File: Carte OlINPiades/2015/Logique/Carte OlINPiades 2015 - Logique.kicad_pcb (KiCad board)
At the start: 2 copper layers, 30 parts, among them U1 dsPIC33FJ128MC802, U2 LM7805, U3 LM2937-3.3

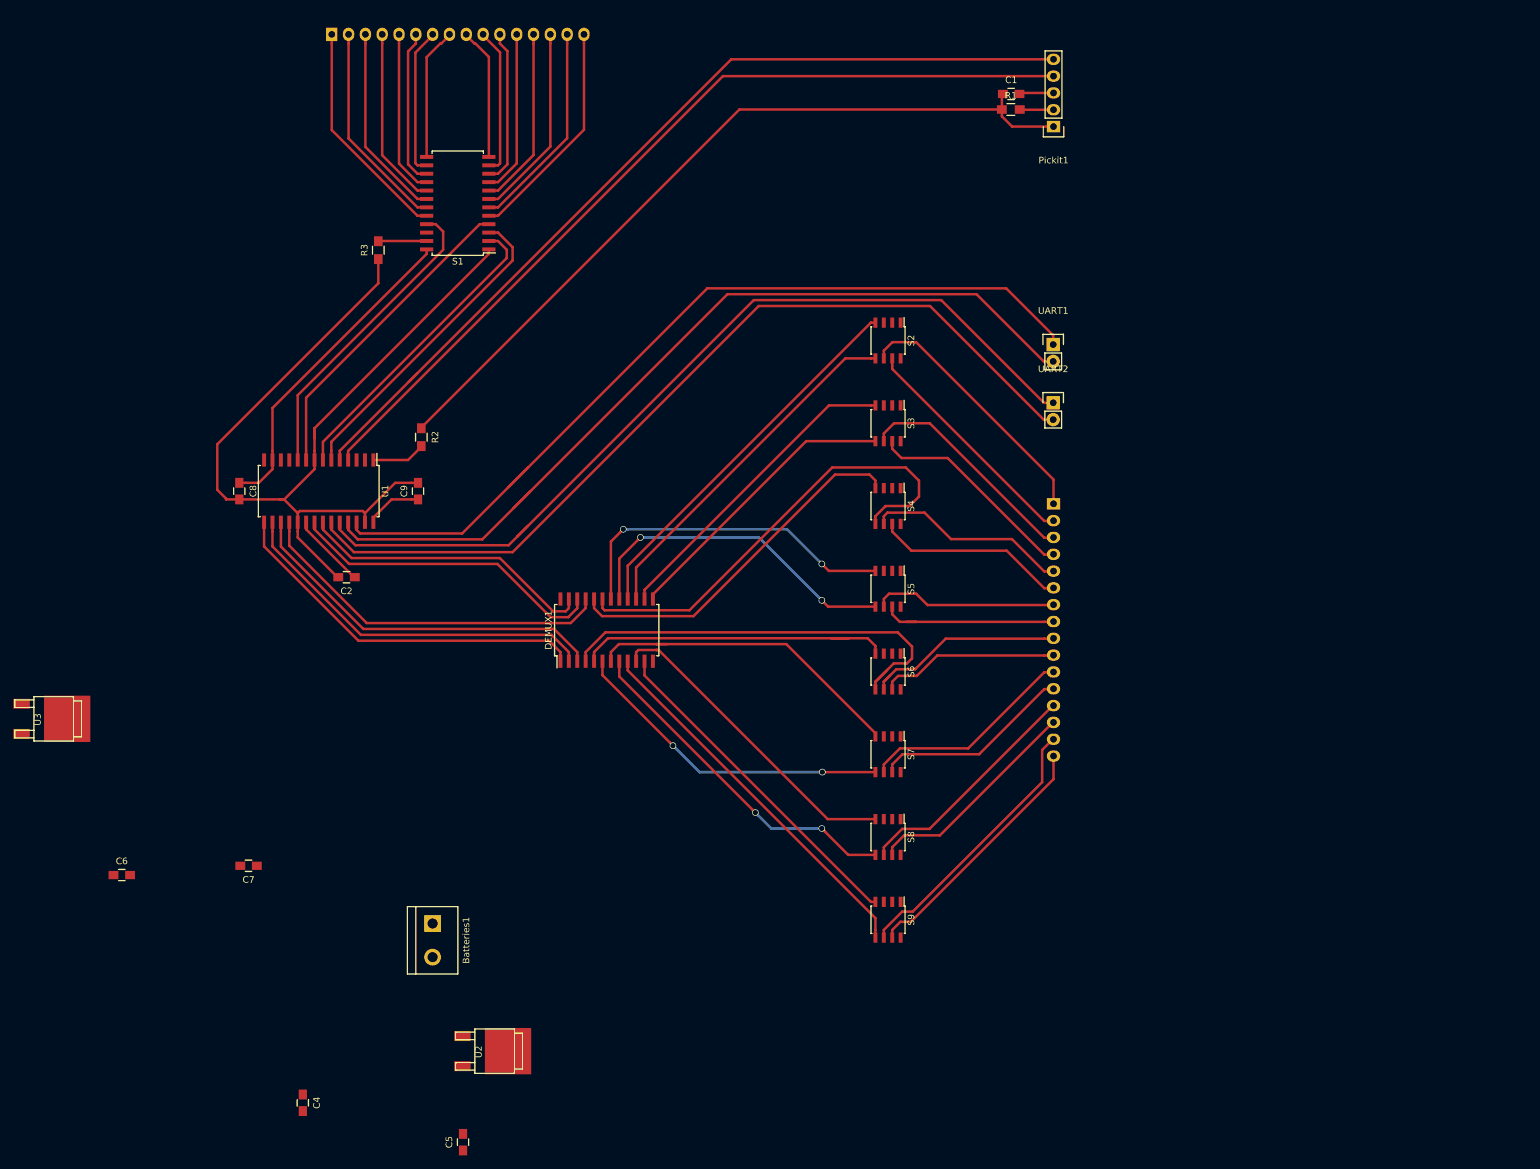
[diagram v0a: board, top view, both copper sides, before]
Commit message: déplace les composant d'alim dans leur zone
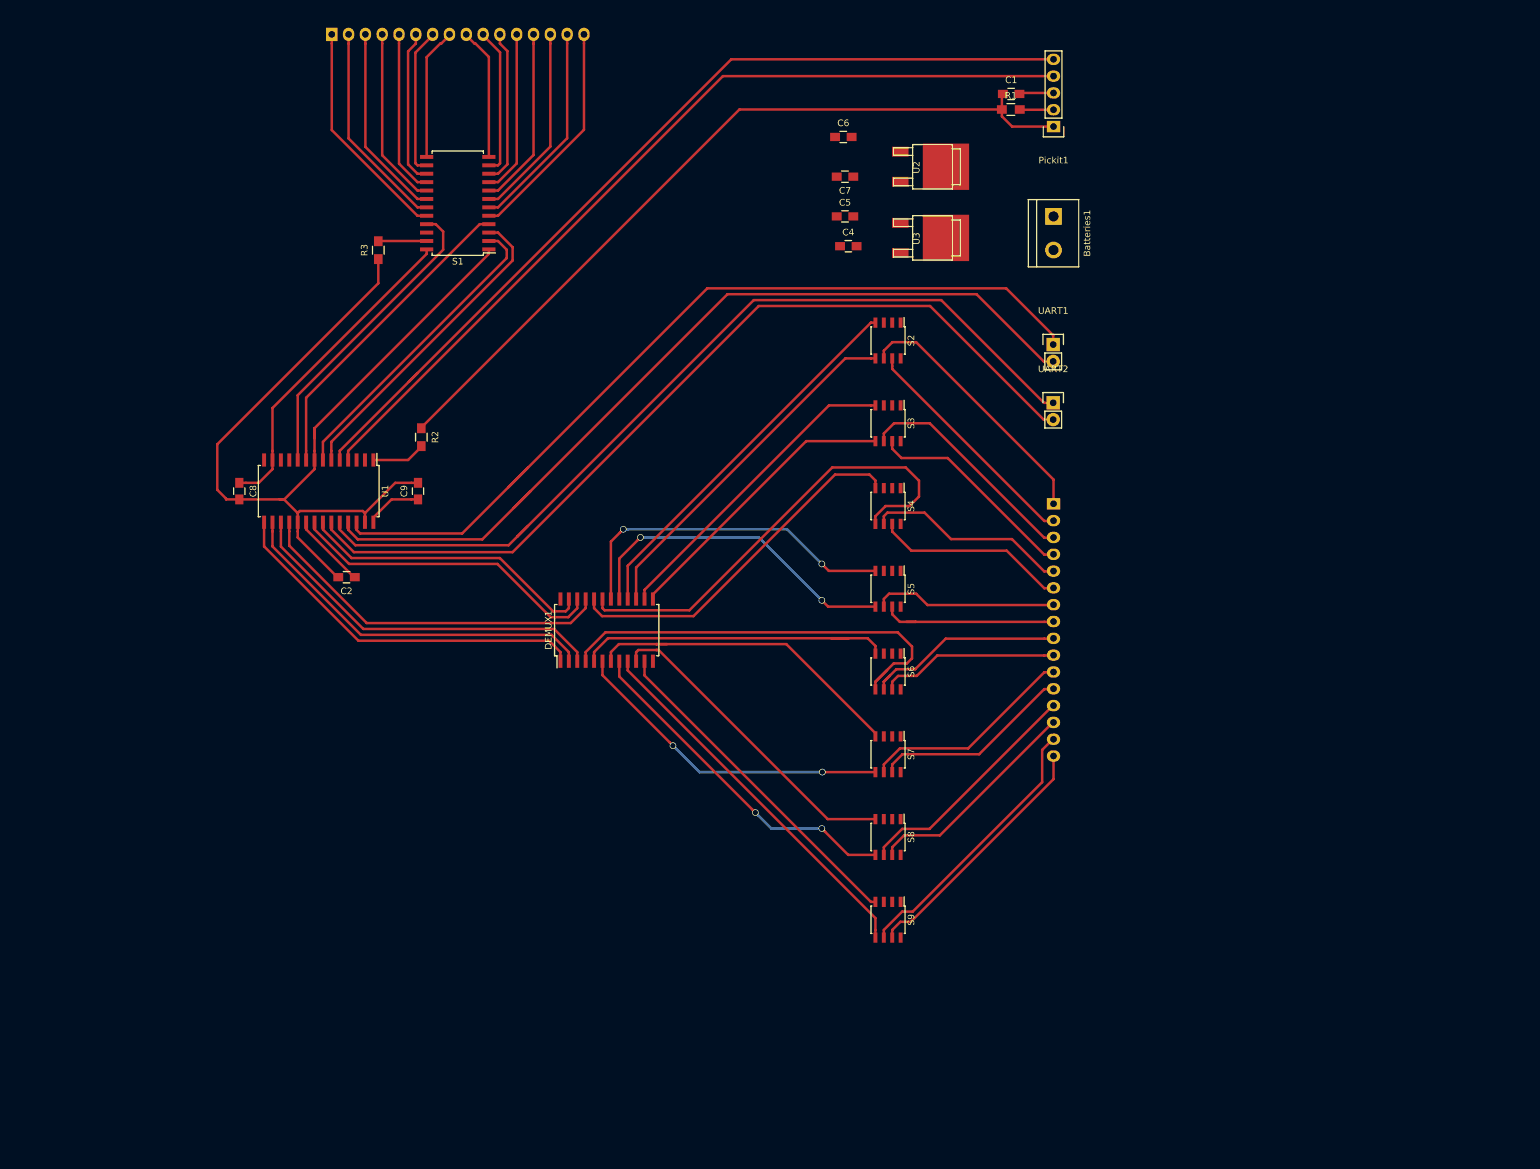
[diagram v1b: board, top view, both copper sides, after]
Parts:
- moved C6 155.9 mm to (198.2, 25.5)
- moved C4 153.4 mm to (199.0, 42.0), turned to 0 degrees
- moved U3 151.3 mm to (210.3, 40.8)
- moved C5 151.3 mm to (198.5, 37.5), turned to 0 degrees
- moved U2 149.1 mm to (210.3, 30.0)
- moved Batteries1 142.2 mm to (230.0, 40.0)
- moved C7 137.7 mm to (198.5, 31.5)
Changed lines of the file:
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@@
     (visible_elements FFFFFF7F)
     (pcbplotparams
-      (layerselection 0x00030_80000001)
+      (layerselection 0x3c000_00000001)
       (usegerberextensions false)
       (excludeedgelayer true)
@@
       (outputformat 1)
       (mirror false)
-      (drillshape 1)
+      (drillshape 0)
       (scaleselection 1)
       (outputdirectory ""))
@@
   )
   (module Capacitors_SMD:C_0805_HandSoldering (layer F.Cu)
-    (at 108.4 135.6 180)
+    (at 198.5 31.5 180)
     (descr "Capacitor SMD 0805, hand soldering")
     (tags "capacitor 0805")
@@
   )
   (module Connect:bornier2 (layer F.Cu)
-    (at 136.2 146.86 270)
+    (at 230 40.04 270)
     (descr "Bornier d'alimentation 2 pins")
     (tags DEV)
@@
   )
   (module Capacitors_SMD:C_0805_HandSoldering (layer F.Cu)
-    (at 116.6 171.4 270)
+    (at 199 42)
     (descr "Capacitor SMD 0805, hand soldering")
     (tags "capacitor 0805")
     (attr smd)
-    (fp_text reference C4 (at 0 -2.1 270) (layer F.SilkS)
-      (effects (font (size 1 1) (thickness 0.15)))
-    )
-    (fp_text value 330nF (at 0 2.1 270) (layer F.Fab)
+    (fp_text reference C4 (at 0 -2.1) (layer F.SilkS)
+      (effects (font (size 1 1) (thickness 0.15)))
+    )
+    (fp_text value 330nF (at 0 2.1) (layer F.Fab)
       (effects (font (size 1 1) (thickness 0.15)))
     )
@@
     (fp_line (start 0.5 -0.85) (end -0.5 -0.85) (layer F.SilkS) (width 0.15))
     (fp_line (start -0.5 0.85) (end 0.5 0.85) (layer F.SilkS) (width 0.15))
-    (pad 1 smd rect (at -1.25 0 270) (size 1.5 1.25) (layers F.Cu F.Paste F.Mask)
+    (pad 1 smd rect (at -1.25 0) (size 1.5 1.25) (layers F.Cu F.Paste F.Mask)
       (net 1 +12V))
-    (pad 2 smd rect (at 1.25 0 270) (size 1.5 1.25) (layers F.Cu F.Paste F.Mask)
+    (pad 2 smd rect (at 1.25 0) (size 1.5 1.25) (layers F.Cu F.Paste F.Mask)
       (net 2 GND))
     (model Capacitors_SMD.3dshapes/C_0805_HandSoldering.wrl
@@
   )
   (module Capacitors_SMD:C_0805_HandSoldering (layer F.Cu)
-    (at 140.8 177.35 90)
+    (at 198.5 37.5)
     (descr "Capacitor SMD 0805, hand soldering")
     (tags "capacitor 0805")
     (attr smd)
-    (fp_text reference C5 (at 0 -2.1 90) (layer F.SilkS)
-      (effects (font (size 1 1) (thickness 0.15)))
-    )
-    (fp_text value 100nF (at 0 2.1 90) (layer F.Fab)
+    (fp_text reference C5 (at 0 -2.1) (layer F.SilkS)
+      (effects (font (size 1 1) (thickness 0.15)))
+    )
+    (fp_text value 100nF (at 0 2.1) (layer F.Fab)
       (effects (font (size 1 1) (thickness 0.15)))
     )
@@
     (fp_line (start 0.5 -0.85) (end -0.5 -0.85) (layer F.SilkS) (width 0.15))
     (fp_line (start -0.5 0.85) (end 0.5 0.85) (layer F.SilkS) (width 0.15))
-    (pad 1 smd rect (at -1.25 0 90) (size 1.5 1.25) (layers F.Cu F.Paste F.Mask)
-      (net 47 +5V))
-    (pad 2 smd rect (at 1.25 0 90) (size 1.5 1.25) (layers F.Cu F.Paste F.Mask)
+    (pad 1 smd rect (at -1.25 0) (size 1.5 1.25) (layers F.Cu F.Paste F.Mask)
+      (net 47 +5V))
+    (pad 2 smd rect (at 1.25 0) (size 1.5 1.25) (layers F.Cu F.Paste F.Mask)
       (net 2 GND))
     (model Capacitors_SMD.3dshapes/C_0805_HandSoldering.wrl
@@
   )
   (module Capacitors_SMD:C_0805_HandSoldering (layer F.Cu)
-    (at 89.25 137)
+    (at 198.25 25.5)
     (descr "Capacitor SMD 0805, hand soldering")
     (tags "capacitor 0805")
@@
   )
   (module Transistors_SMD:sot428 (layer F.Cu)
-    (at 144.15068 163.6 270)
+    (at 210.30068 30 270)
     (descr SOT428)
     (attr smd)
@@
   )
   (module Transistors_SMD:sot428 (layer F.Cu)
-    (at 77.55068 113.4 270)
+    (at 210.30068 40.75 270)
     (descr SOT428)
     (attr smd)

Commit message: connection logique avec regul ok
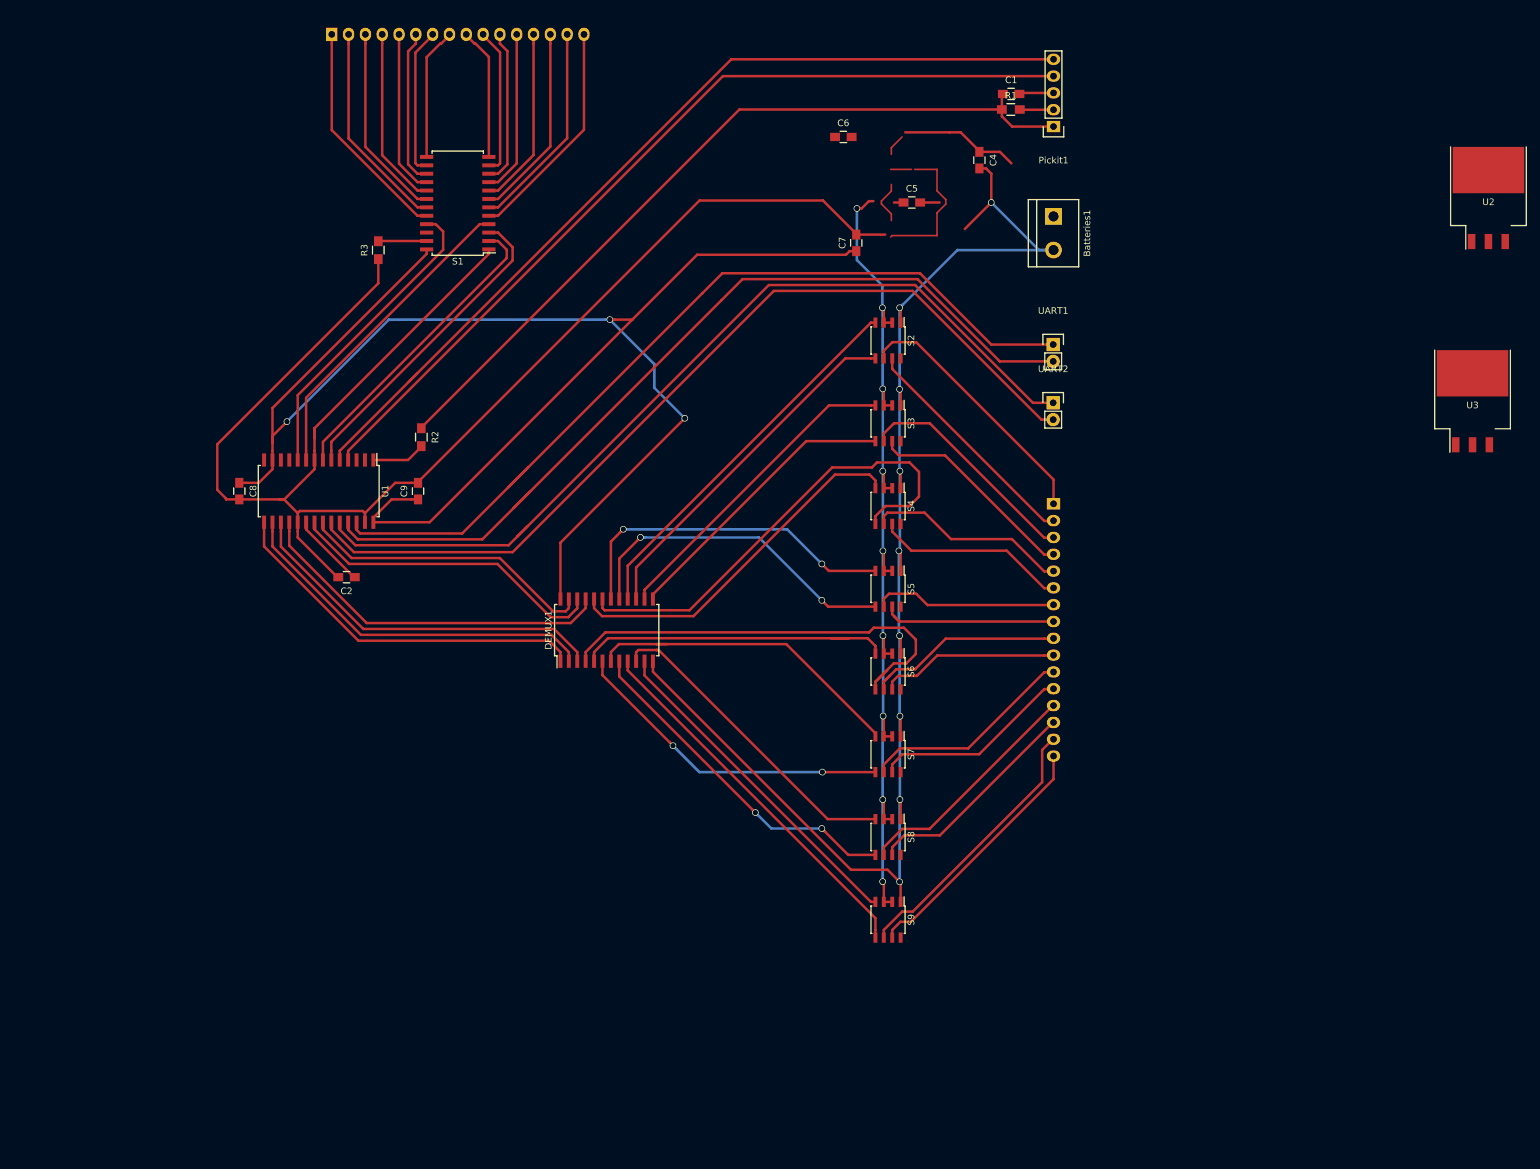
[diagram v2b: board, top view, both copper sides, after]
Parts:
- U2: value LM7805 -> 7805; footprint Transistors_SMD:sot428 -> SMD_Packages:TO-263
- U3: footprint Transistors_SMD:sot428 -> SMD_Packages:TO-263
- moved U3 88.7 mm to (293.3, 72.0), turned to 0 degrees
- moved U2 86.1 mm to (295.7, 41.3), turned to 0 degrees
- moved C4 23.7 mm to (218.8, 29.0), turned to 270 degrees
- moved C5 10.3 mm to (208.6, 35.4)
- moved C7 10.1 mm to (200.2, 41.5), turned to 90 degrees
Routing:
- net GND: track 150.6 -> 457.1 mm, vias 0 -> 9
- net +3.3V: track 62.6 -> 269.8 mm, vias 0 -> 3
- net +5V: track 0.00 -> 140.6 mm, vias 0 -> 9
- net (no net): track 0.00 -> 34.7 mm
- net +12V: track 0.00 -> 18.0 mm
- net Net-(DEMUX1-Pad4): track 65.2 -> 67.2 mm
- net RB14: track 131.3 -> 133.2 mm
- net RB12: track 134.1 -> 136.0 mm
- net RB13: track 133.9 -> 135.8 mm
- net Net-(DEMUX1-Pad19): track 70.5 -> 71.9 mm
- net RB15: track 130.4 -> 131.5 mm

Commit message: cablage alim
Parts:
- removed C5: 100nF, Capacitors_SMD:C_0805_HandSoldering
- C4, C6, C7, U2, U3: moved to B.Cu
- moved U3 104.9 mm to (194.2, 37.6), turned to 180 degrees
- moved U2 88.0 mm to (207.8, 37.6), turned to 180 degrees
- moved C6 13.1 mm to (201.0, 38.3), turned to 90 degrees
- moved C4 11.2 mm to (217.4, 40.1)
- moved C7 7.20 mm to (193.0, 41.5), turned to 0 degrees
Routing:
- net GND: track 457.1 -> 701.7 mm
- net +3.3V: track 269.8 -> 341.9 mm
- net (no net): track 34.7 -> 0.00 mm
- net +12V: track 18.0 -> 21.1 mm
- net +5V: track 140.6 -> 143.3 mm, vias 9 -> 8

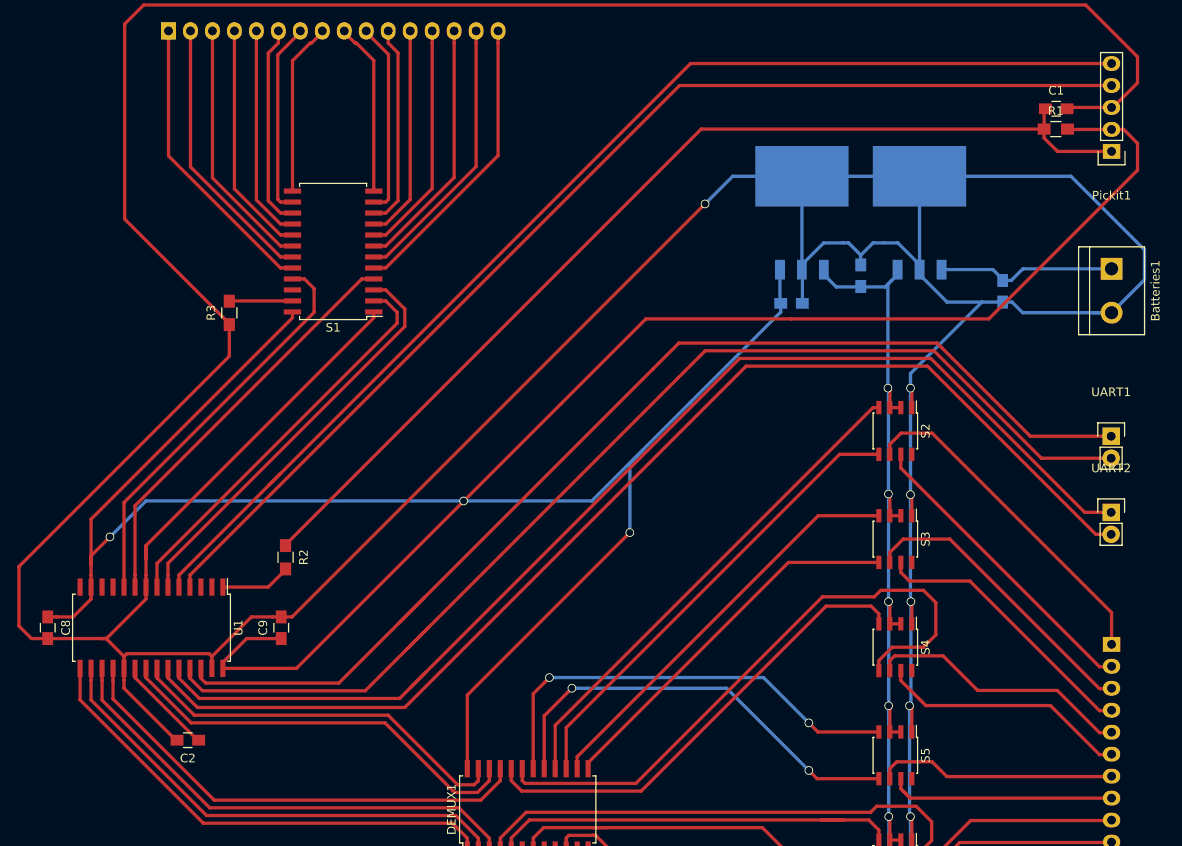
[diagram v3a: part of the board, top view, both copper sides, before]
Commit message: DRC ok sauf pour connecteur d'UART ?
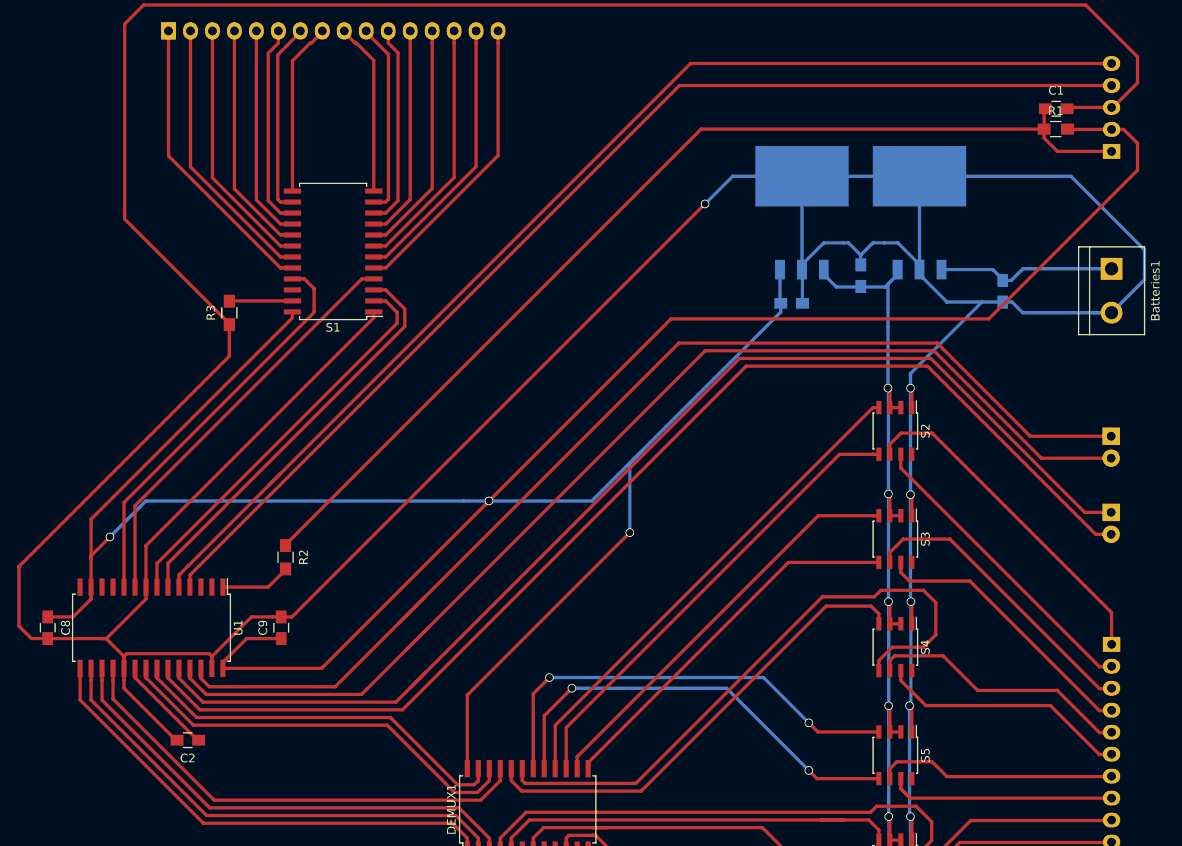
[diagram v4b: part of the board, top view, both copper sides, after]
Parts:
- Pickit1, UART1, UART2: moved to B.Cu
- turned Pickit1 to 0 degrees
- turned UART1 to 180 degrees
- turned UART2 to 180 degrees
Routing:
- net GND: track 701.7 -> 700.2 mm
- net +3.3V: track 341.9 -> 341.0 mm
